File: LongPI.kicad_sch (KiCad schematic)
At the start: 0 parts

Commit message: Add parts to sch, pcb
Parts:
- added J1: USB_C_Receptacle_USB2.0, Connector_USB:USB_C_Receptacle_G-Switch_GT-USB-7010ASV, symbol Connector:USB_C_Receptacle_USB2.0
- added J2: Conn_01x30, Connector_PinHeader_2.54mm:PinHeader_2x30_P2.54mm_Vertical, symbol Connector_Generic:Conn_01x30
- added U1: RP2040, Package_DFN_QFN:QFN-56-1EP_7x7mm_P0.4mm_EP3.2x3.2mm, symbol MCU_RaspberryPi:RP2040
- added U2: USBLC6-2SC6, Package_TO_SOT_SMD:SOT-23-6, symbol Power_Protection:USBLC6-2SC6
- added U3: XC6210B332MR, Package_TO_SOT_SMD:SOT-23-5, symbol Regulator_Linear:XC6210B332MR
- added U4: W25Q128JVS, Package_SO:SOIC-8_5.23x5.23mm_P1.27mm, symbol Memory_Flash:W25Q128JVS
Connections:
- new net: U1.1 (IOVDD), U1.10 (IOVDD), U1.22 (IOVDD), U1.33 (IOVDD), U1.42 (IOVDD), U1.49 (IOVDD)
- new net: U1.23 (DVDD), U1.50 (DVDD)
- new net: J1.A1 (GND), J1.A12 (GND), J1.B1 (GND), J1.B12 (GND)
- new net: J1.A4 (VBUS), J1.A9 (VBUS), J1.B4 (VBUS), J1.B9 (VBUS)

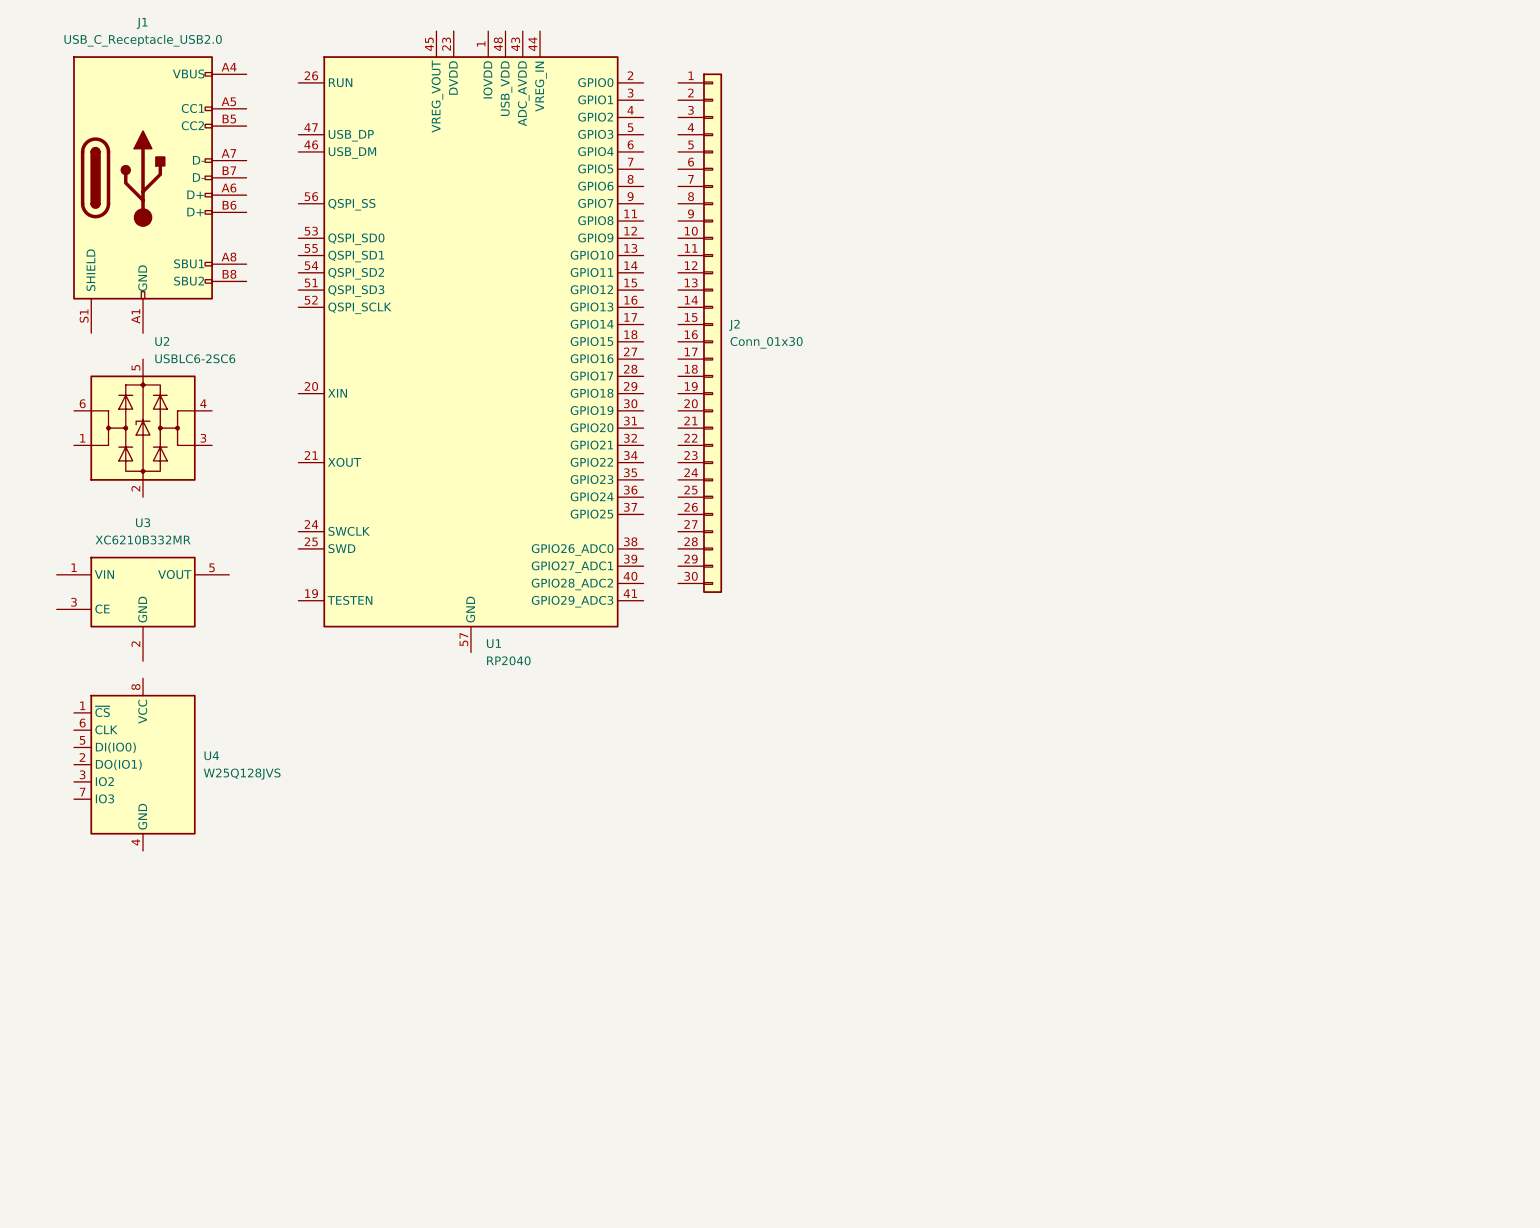
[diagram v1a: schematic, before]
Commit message: USB-C setup on sch
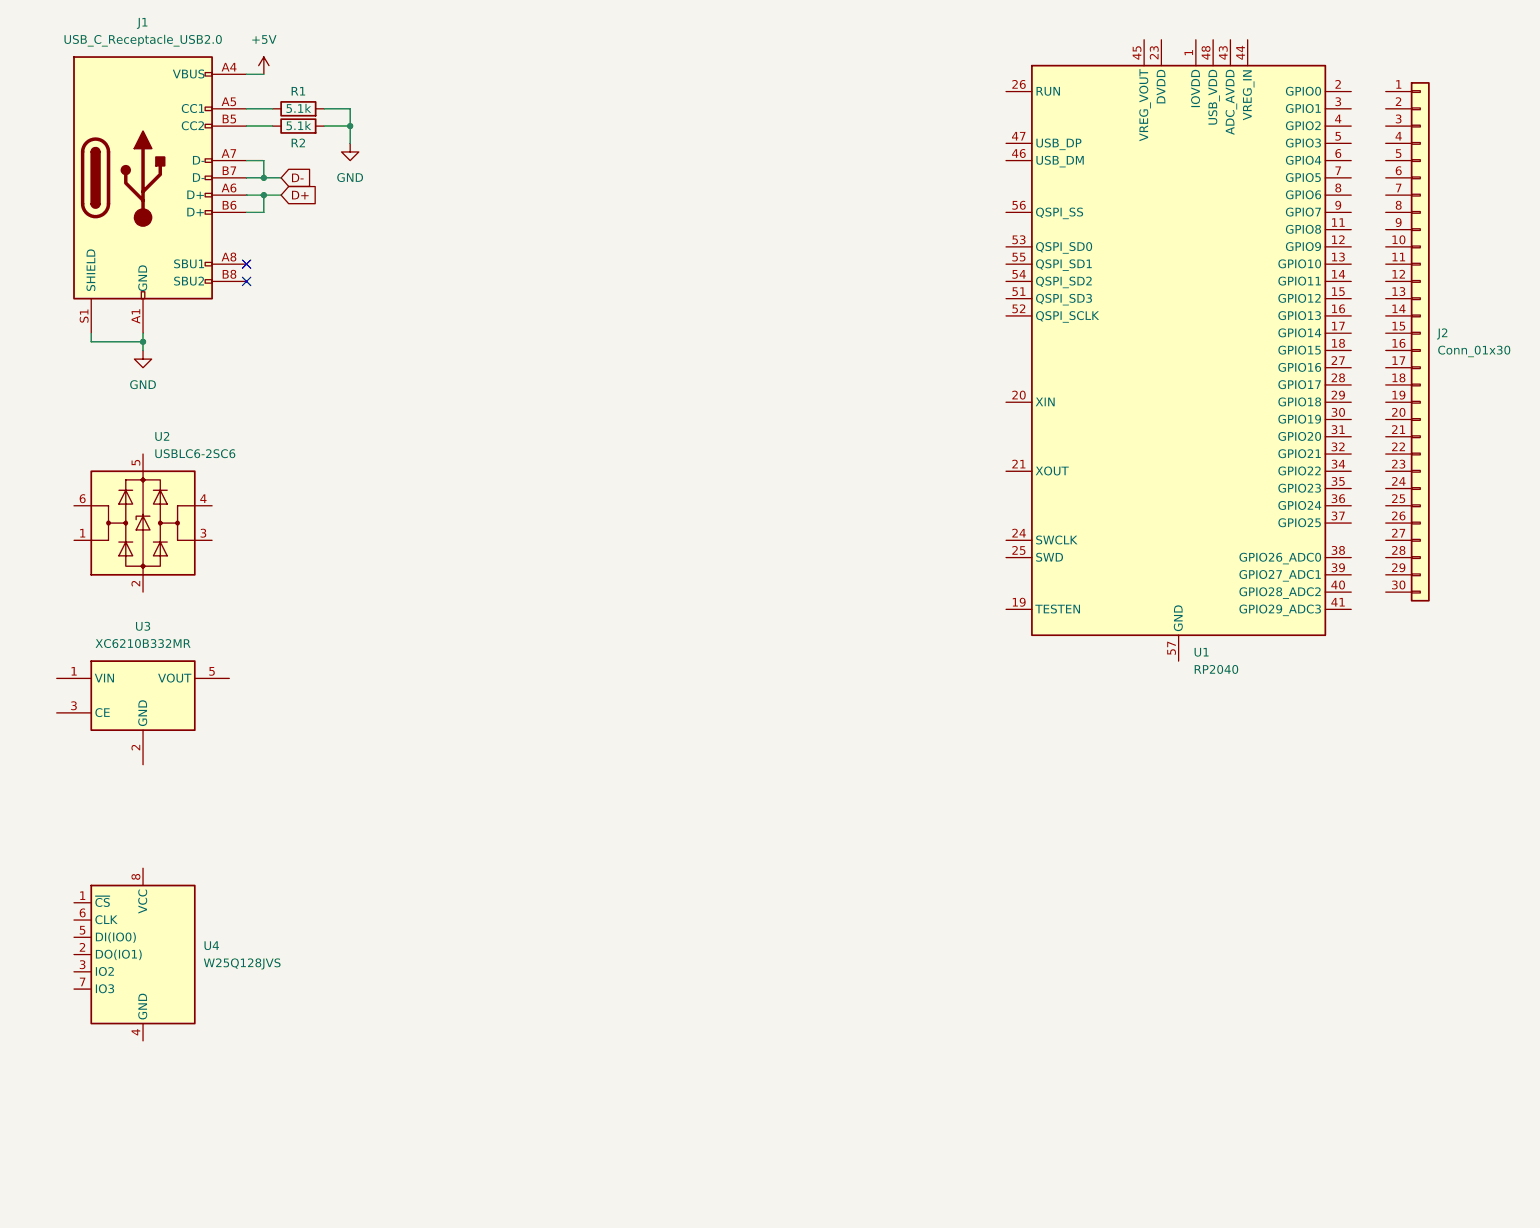
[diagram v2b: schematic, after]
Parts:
- added R1, R2: 5.1k, symbol Device:R
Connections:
- net GND: now reaches J1.A1 (GND), J1.A12 (GND), J1.B1 (GND), J1.B12 (GND)
- net GND: now also J1.S1 (SHIELD), R1.2, R2.2
- net +5V: now reaches J1.A4 (VBUS), J1.A9 (VBUS), J1.B4 (VBUS), J1.B9 (VBUS)
- net at J1.A5 (CC1): now also R1.1
- net D+: now reaches J1.A6 (D+)
- net D+: now also J1.B6 (D+)
- net D-: now reaches J1.A7 (D-)
- net D-: now also J1.B7 (D-)
- net at J1.B5 (CC2): now also R2.1
- no-connect marks 0 -> 2
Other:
- moved on the sheet: J2, U1, U2, U3, U4

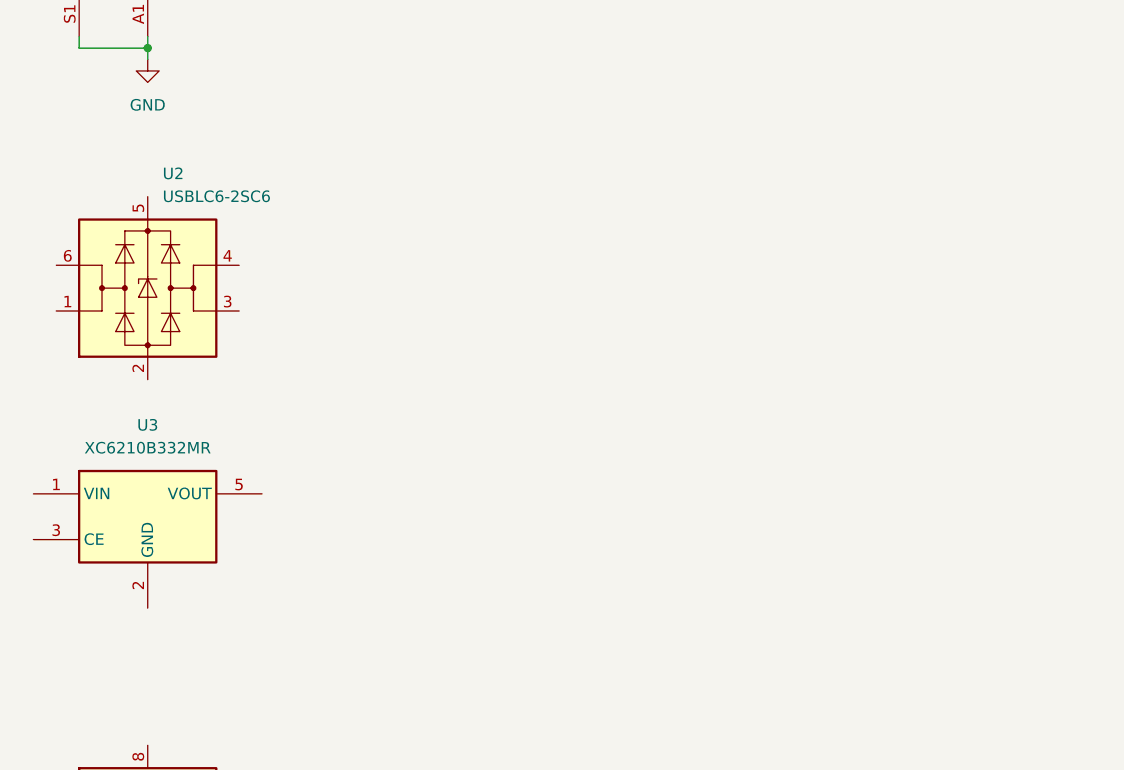
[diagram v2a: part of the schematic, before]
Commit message: Voltage regulator setup on sch
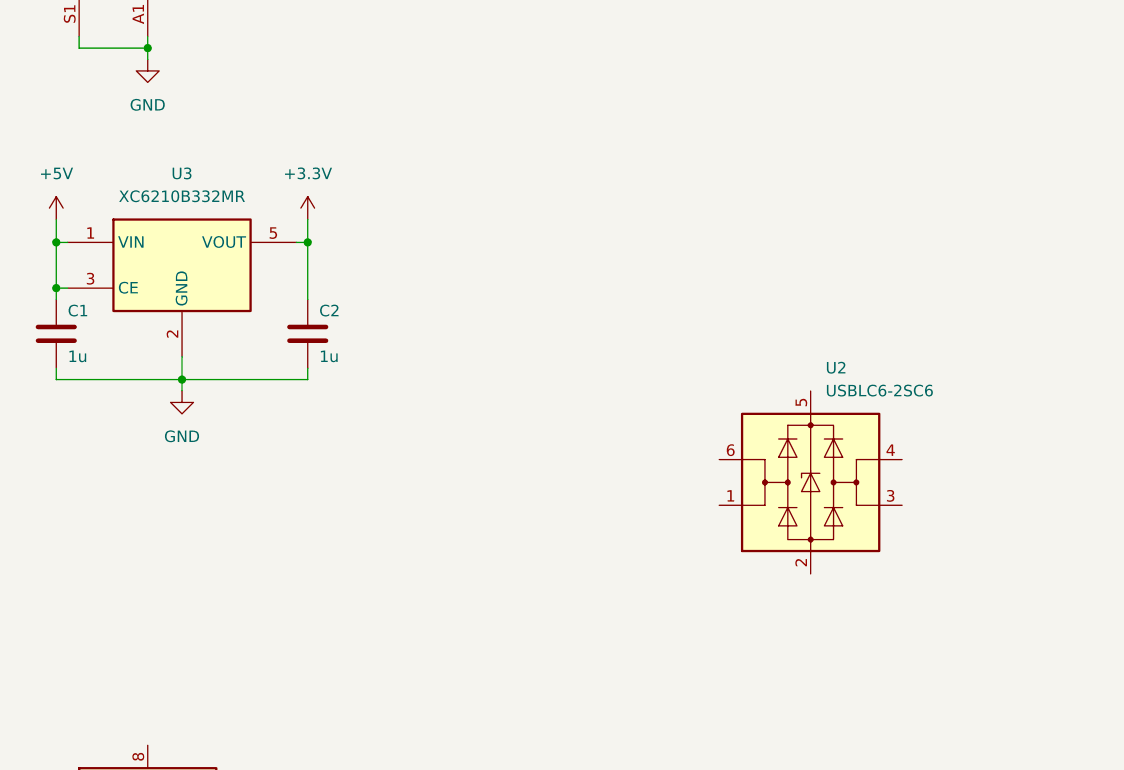
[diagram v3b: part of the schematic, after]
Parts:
- added C1, C2: 1u, symbol Device:C
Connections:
- net +5V: now also U3.1 (VIN), U3.3 (CE), C1.1
- net GND: now also U3.2 (GND), C1.2, C2.2
- net +3.3V: now reaches U3.5 (VOUT)
- net +3.3V: now also C2.1
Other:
- moved on the sheet: U2, U3
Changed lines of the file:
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@@
 (kicad_sch (version 20230121) (generator eeschema)
   (paper "A4")
+  (junction (at 39.37 100.33) (diameter 0) (color 0 0 0 0)
+  )
+  (junction (at 25.4 85.09) (diameter 0) (color 0 0 0 0)
+  )
   (junction (at 53.34 39.37) (diameter 0) (color 0 0 0 0)
   )
   (junction (at 35.56 63.5) (diameter 0) (color 0 0 0 0)
+  )
+  (junction (at 25.4 90.17) (diameter 0) (color 0 0 0 0)
+  )
+  (junction (at 53.34 85.09) (diameter 0) (color 0 0 0 0)
   )
   (junction (at 66.04 31.75) (diameter 0) (color 0 0 0 0)
@@
     (stroke (width 0) (type default))
   )
+  (wire (pts (xy 39.37 100.33) (xy 39.37 101.6))
+    (stroke (width 0) (type default))
+  )
+  (wire (pts (xy 53.34 100.33) (xy 53.34 99.06))
+    (stroke (width 0) (type default))
+  )
+  (wire (pts (xy 53.34 85.09) (xy 52.07 85.09))
+    (stroke (width 0) (type default))
+  )
+  (wire (pts (xy 25.4 85.09) (xy 26.67 85.09))
+    (stroke (width 0) (type default))
+  )
   (wire (pts (xy 35.56 63.5) (xy 35.56 64.77))
     (stroke (width 0) (type default))
   )
+  (wire (pts (xy 25.4 82.55) (xy 25.4 85.09))
+    (stroke (width 0) (type default))
+  )
   (wire (pts (xy 66.04 31.75) (xy 66.04 34.29))
     (stroke (width 0) (type default))
@@
     (stroke (width 0) (type default))
   )
+  (wire (pts (xy 25.4 91.44) (xy 25.4 90.17))
+    (stroke (width 0) (type default))
+  )
   (wire (pts (xy 53.34 41.91) (xy 55.88 41.91))
     (stroke (width 0) (type default))
@@
     (stroke (width 0) (type default))
   )
+  (wire (pts (xy 39.37 100.33) (xy 53.34 100.33))
+    (stroke (width 0) (type default))
+  )
+  (wire (pts (xy 39.37 97.79) (xy 39.37 100.33))
+    (stroke (width 0) (type default))
+  )
+  (wire (pts (xy 25.4 85.09) (xy 25.4 90.17))
+    (stroke (width 0) (type default))
+  )
+  (wire (pts (xy 25.4 100.33) (xy 25.4 99.06))
+    (stroke (width 0) (type default))
+  )
+  (wire (pts (xy 53.34 82.55) (xy 53.34 85.09))
+    (stroke (width 0) (type default))
+  )
   (wire (pts (xy 53.34 44.45) (xy 53.34 41.91))
     (stroke (width 0) (type default))
@@
     (stroke (width 0) (type default))
   )
+  (wire (pts (xy 25.4 90.17) (xy 26.67 90.17))
+    (stroke (width 0) (type default))
+  )
   (wire (pts (xy 53.34 39.37) (xy 55.88 39.37))
     (stroke (width 0) (type default))
   )
+  (wire (pts (xy 53.34 85.09) (xy 53.34 91.44))
+    (stroke (width 0) (type default))
+  )
   (wire (pts (xy 66.04 29.21) (xy 66.04 31.75))
     (stroke (width 0) (type default))
@@
   )
   (wire (pts (xy 62.23 31.75) (xy 66.04 31.75))
+    (stroke (width 0) (type default))
+  )
+  (wire (pts (xy 25.4 100.33) (xy 39.37 100.33))
     (stroke (width 0) (type default))
   )
@@
     )
   )
+  (symbol (lib_id "Device:C") (at 25.4 95.25 0) (unit 1)
+    (in_bom yes) (on_board yes) (dnp no)
+    (property "Reference" "C1" (at 26.67 92.71 0)
+      (effects (font (size 1.27 1.27)) (justify left))
+    )
+    (property "Value" "1u" (at 26.67 97.79 0)
+      (effects (font (size 1.27 1.27)) (justify left))
+    )
+    (property "Footprint" "" (at 26.3652 99.06 0)
+      (effects (font (size 1.27 1.27)) hide)
+    )
+    (property "Datasheet" "~" (at 25.4 95.25 0)
+      (effects (font (size 1.27 1.27)) hide)
+    )
+    (pin "1")
+    (pin "2")
+    (instances
+      (project "LongPI"
+        (path "/cc33761c-f139-4a76-bdf7-f72d959ddb3d"
+          (reference "C1") (unit 1)
+        )
+      )
+    )
+  )
+  (symbol (lib_id "Device:C") (at 53.34 95.25 0) (unit 1)
+    (in_bom yes) (on_board yes) (dnp no)
+    (property "Reference" "C2" (at 54.61 92.71 0)
+      (effects (font (size 1.27 1.27)) (justify left))
+    )
+    (property "Value" "1u" (at 54.61 97.79 0)
+      (effects (font (size 1.27 1.27)) (justify left))
+    )
+    (property "Footprint" "" (at 54.3052 99.06 0)
+      (effects (font (size 1.27 1.27)) hide)
+    )
+    (property "Datasheet" "~" (at 53.34 95.25 0)
+      (effects (font (size 1.27 1.27)) hide)
+    )
+    (pin "1")
+    (pin "2")
+    (instances
+      (project "LongPI"
+        (path "/cc33761c-f139-4a76-bdf7-f72d959ddb3d"
+          (reference "C2") (unit 1)
+        )
+      )
+    )
+  )
   (symbol (lib_id "power:GND") (at 66.04 34.29 0) (unit 1)
     (in_bom yes) (on_board yes) (dnp no) (fields_autoplaced)
@@
         (path "/cc33761c-f139-4a76-bdf7-f72d959ddb3d"
           (reference "#PWR01") (unit 1)
+        )
+      )
+    )
+  )
+  (symbol (lib_id "power:+5V") (at 25.4 82.55 0) (unit 1)
+    (in_bom yes) (on_board yes) (dnp no) (fields_autoplaced)
+    (property "Reference" "#PWR04" (at 25.4 86.36 0)
+      (effects (font (size 1.27 1.27)) hide)
+    )
+    (property "Value" "+5V" (at 25.4 77.47 0)
+      (effects (font (size 1.27 1.27)))
+    )
+    (property "Footprint" "" (at 25.4 82.55 0)
+      (effects (font (size 1.27 1.27)) hide)
+    )
+    (property "Datasheet" "" (at 25.4 82.55 0)
+      (effects (font (size 1.27 1.27)) hide)
+    )
+    (pin "1")
+    (instances
+      (project "LongPI"
+        (path "/cc33761c-f139-4a76-bdf7-f72d959ddb3d"
+          (reference "#PWR04") (unit 1)
         )
       )
@@
     )
   )
-  (symbol (lib_id "Regulator_Linear:XC6210B332MR") (at 35.56 115.57 0) (unit 1)
-    (in_bom yes) (on_board yes) (dnp no) (fields_autoplaced)
-    (property "Reference" "U3" (at 35.56 105.41 0)
-      (effects (font (size 1.27 1.27)))
-    )
-    (property "Value" "XC6210B332MR" (at 35.56 107.95 0)
-      (effects (font (size 1.27 1.27)))
-    )
-    (property "Footprint" "Package_TO_SOT_SMD:SOT-23-5" (at 35.56 115.57 0)
-      (effects (font (size 1.27 1.27)) hide)
-    )
-    (property "Datasheet" "https://www.torexsemi.com/file/xc6210/XC6210.pdf" (at 54.61 140.97 0)
+  (symbol (lib_id "Regulator_Linear:XC6210B332MR") (at 39.37 87.63 0) (unit 1)
+    (in_bom yes) (on_board yes) (dnp no) (fields_autoplaced)
+    (property "Reference" "U3" (at 39.37 77.47 0)
+      (effects (font (size 1.27 1.27)))
+    )
+    (property "Value" "XC6210B332MR" (at 39.37 80.01 0)
+      (effects (font (size 1.27 1.27)))
+    )
+    (property "Footprint" "Package_TO_SOT_SMD:SOT-23-5" (at 39.37 87.63 0)
+      (effects (font (size 1.27 1.27)) hide)
+    )
+    (property "Datasheet" "https://www.torexsemi.com/file/xc6210/XC6210.pdf" (at 58.42 113.03 0)
       (effects (font (size 1.27 1.27)) hide)
     )
@@
         (path "/cc33761c-f139-4a76-bdf7-f72d959ddb3d"
           (reference "J1") (unit 1)
+        )
+      )
+    )
+  )
+  (symbol (lib_id "power:GND") (at 39.37 101.6 0) (unit 1)
+    (in_bom yes) (on_board yes) (dnp no) (fields_autoplaced)
+    (property "Reference" "#PWR05" (at 39.37 107.95 0)
+      (effects (font (size 1.27 1.27)) hide)
+    )
+    (property "Value" "GND" (at 39.37 106.68 0)
+      (effects (font (size 1.27 1.27)))
+    )
+    (property "Footprint" "" (at 39.37 101.6 0)
+      (effects (font (size 1.27 1.27)) hide)
+    )
+    (property "Datasheet" "" (at 39.37 101.6 0)
+      (effects (font (size 1.27 1.27)) hide)
+    )
+    (pin "1")
+    (instances
+      (project "LongPI"
+        (path "/cc33761c-f139-4a76-bdf7-f72d959ddb3d"
+          (reference "#PWR05") (unit 1)
         )
       )
@@
     )
   )
+  (symbol (lib_id "power:+3.3V") (at 53.34 82.55 0) (unit 1)
+    (in_bom yes) (on_board yes) (dnp no) (fields_autoplaced)
+    (property "Reference" "#PWR06" (at 53.34 86.36 0)
+      (effects (font (size 1.27 1.27)) hide)
+    )
+    (property "Value" "+3.3V" (at 53.34 77.47 0)
+      (effects (font (size 1.27 1.27)))
+    )
+    (property "Footprint" "" (at 53.34 82.55 0)
+      (effects (font (size 1.27 1.27)) hide)
+    )
+    (property "Datasheet" "" (at 53.34 82.55 0)
+      (effects (font (size 1.27 1.27)) hide)
+    )
+    (pin "1")
+    (instances
+      (project "LongPI"
+        (path "/cc33761c-f139-4a76-bdf7-f72d959ddb3d"
+          (reference "#PWR06") (unit 1)
+        )
+      )
+    )
+  )
   (symbol (lib_id "power:+5V") (at 53.34 24.13 0) (unit 1)
     (in_bom yes) (on_board yes) (dnp no) (fields_autoplaced)
@@
     )
   )
-  (symbol (lib_id "Power_Protection:USBLC6-2SC6") (at 35.56 90.17 0) (unit 1)
-    (in_bom yes) (on_board yes) (dnp no) (fields_autoplaced)
-    (property "Reference" "U2" (at 37.2111 77.47 0)
-      (effects (font (size 1.27 1.27)) (justify left))
-    )
-    (property "Value" "USBLC6-2SC6" (at 37.2111 80.01 0)
-      (effects (font (size 1.27 1.27)) (justify left))
-    )
-    (property "Footprint" "Package_TO_SOT_SMD:SOT-23-6" (at 35.56 102.87 0)
-      (effects (font (size 1.27 1.27)) hide)
-    )
-    (property "Datasheet" "https://www.st.com/resource/en/datasheet/usblc6-2.pdf" (at 40.64 81.28 0)
-      (effects (font (size 1.27 1.27)) hide)
-    )
+  (symbol (lib_id "Power_Protection:USBLC6-2SC6") (at 109.22 111.76 0) (unit 1)
+    (in_bom yes) (on_board yes) (dnp no) (fields_autoplaced)
+    (property "Reference" "U2" (at 110.8711 99.06 0)
+      (effects (font (size 1.27 1.27)) (justify left))
+    )
+    (property "Value" "USBLC6-2SC6" (at 110.8711 101.6 0)
+      (effects (font (size 1.27 1.27)) (justify left))
+    )
+    (property "Footprint" "Package_TO_SOT_SMD:SOT-23-6" (at 109.22 124.46 0)
+      (effects (font (size 1.27 1.27)) hide)
+    )
+    (property "Datasheet" "https://www.st.com/resource/en/datasheet/usblc6-2.pdf" (at 114.3 102.87 0)
+      (effects (font (size 1.27 1.27)) hide)
+    )
